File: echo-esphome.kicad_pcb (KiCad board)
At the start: 2 copper layers, 160 x 100 mm, 4 parts

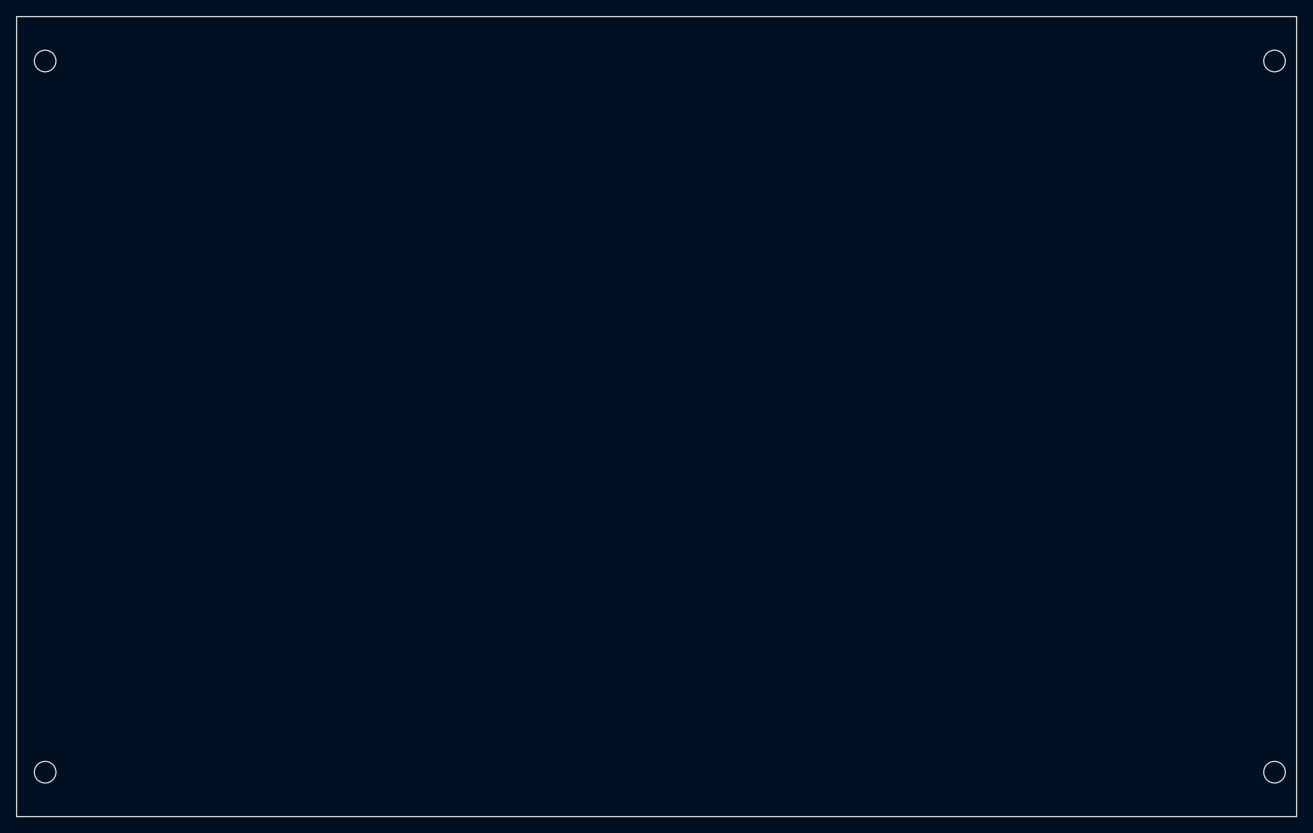
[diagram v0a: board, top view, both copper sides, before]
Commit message: Documentation and basic board layout
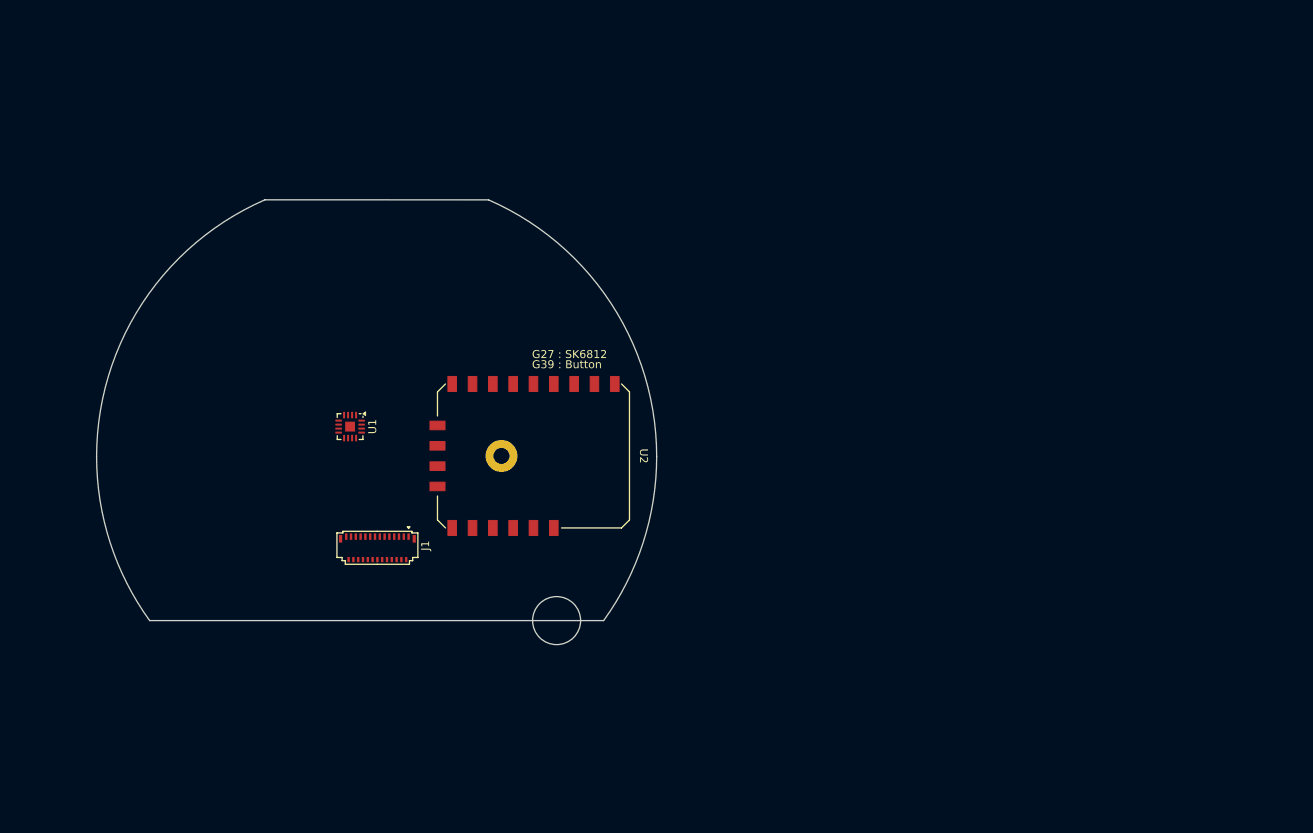
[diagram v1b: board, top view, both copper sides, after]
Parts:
- removed MH1, MH2, MH3, MH4: MountingHole_2.7mm_M2.5_DIN965, MountingHole:MountingHole_2.7mm_M2.5_DIN965
- added J1: Conn_01x27_Pin, Connector_FFC-FPC:Hirose_FH26-27S-0.3SHW_2Rows-27Pins-1MP_P0.60mm_Horizontal, F.Cu at (100.1, 111.4)
- added U1: MAX98357A, Package_DFN_QFN:TQFN-16-1EP_3x3mm_P0.5mm_EP1.23x1.23mm, F.Cu at (96.7, 96.2)
- added U2: M5STAMP-PICO, Boad_dev:M5STAMP-PICO, F.Cu at (115.6, 99.9)
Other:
- board size 160 x 100 mm -> 70 x 55.6 mm
- board text added: "Board"
- board text added: "Inner"
- board text added: "Outer"
- board text removed: "Mounting holes are optional Keepout areas are for for guide rails"
